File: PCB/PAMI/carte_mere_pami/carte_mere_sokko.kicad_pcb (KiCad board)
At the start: 2 copper layers, 78.5 x 66.5 mm, 34 parts, among them IC1 ESP32-S3-WROOM-1-N16R8, IC2 LDO_3.3V_bis, J1 Conn_01x08_Socket, J10 Conn_01x07_Socket, J11 Conn_01x07_Socket, J12 Conn_Servos, J14 LiDAR Connector, J2 Connector 5V, J3 Connector 3.3V, J4 Micro_USB_pads_USB3075-30-A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

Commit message: Routing nearly done
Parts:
- removed J6, J7: Conn_01x04_Socket, Connector_PinHeader_2.54mm:PinHeader_1x04_P2.54mm_Vertical
- moved TP_3.3V1 54.5 mm to (131.0, 82.5)
- moved D1 50.9 mm to (135.0, 89.5), turned to 90 degrees
- moved C9 49.6 mm to (135.0, 93.0), turned to -90 degrees
- moved TP_5V_USB1 48.5 mm to (138.0, 91.0)
- moved J3 43.5 mm to (135.0, 72.5), turned to -90 degrees
- moved C10 41.7 mm to (134.0, 85.0), turned to 180 degrees
- moved J1 38.0 mm to (181.5, 113.0), turned to 90 degrees
- moved J12 37.9 mm to (198.5, 80.0)
- moved J10 37.6 mm to (139.5, 101.3)
- moved C11 36.3 mm to (202.5, 87.5), turned to -90 degrees
- moved C7 34.9 mm to (205.0, 87.5), turned to -90 degrees
- moved J2 33.2 mm to (144.0, 72.5), turned to -90 degrees
- moved J5 32.5 mm to (181.5, 102.0), turned to 90 degrees
- moved C5 31.9 mm to (198.4, 109.5)
- moved J11 31.3 mm to (154.0, 101.4)
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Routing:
- net GND: track 0.00 -> 129.4 mm
- net MISO_LoRa: track 0.00 -> 67.0 mm
- net +3.3V: track 0.00 -> 63.0 mm
- net SS_LoRa: track 0.00 -> 57.1 mm
- net RS-SW_LoRa: track 0.00 -> 37.4 mm
- net EN_Right: track 0.00 -> 36.5 mm
- net RST_LoRa: track 0.00 -> 33.5 mm
- net Busy_LoRa: track 0.00 -> 32.3 mm
- net MOSI_LoRa: track 0.00 -> 31.7 mm
- net Boot_Button: track 0.00 -> 31.3 mm
- net DIO1_LoRa: track 0.00 -> 31.0 mm
- net CLK_LoRa: track 0.00 -> 30.7 mm
- net Data_servo: track 0.00 -> 30.4 mm
- net RX_LiDAR: track 0.00 -> 30.0 mm
- net EN_Left: track 0.00 -> 29.9 mm, vias 0 -> 2
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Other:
- outline, holes or cut-outs redrawn

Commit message: Smaller
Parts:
- added J6: Conn_01x04_Socket, Connector_PinHeader_2.54mm:PinHeader_1x04_P2.54mm_Vertical, F.Cu at (181.2, 114.0)
- added J7: Conn_01x04_Socket, Connector_PinHeader_2.54mm:PinHeader_1x04_P2.54mm_Vertical, F.Cu at (157.7, 114.0)
- moved TP_3.3V1 19.5 mm to (150.0, 78.0)
- moved J4 16.7 mm to (131.4, 83.4)
- moved C9 16.3 mm to (145.5, 80.5), turned to 0 degrees
- moved TP_5V_USB1 14.5 mm to (148.5, 81.0)
- moved IC2 12.3 mm to (142.5, 83.5), turned to 0 degrees
- moved D1 11.4 mm to (142.0, 80.5), turned to 180 degrees
- moved J10 10.6 mm to (133.0, 93.0)
- moved J11 10.6 mm to (147.5, 93.0)
- moved J1 7.11 mm to (176.0, 108.5)
- moved J5 7.11 mm to (176.0, 97.5)
- moved J8 7.11 mm to (153.0, 108.5)
- moved J9 7.11 mm to (153.0, 97.5)
- moved C10 4.95 mm to (137.5, 81.5), turned to -90 degrees
- moved C5 4.53 mm to (195.0, 112.5)
- moved C6 4.19 mm to (171.5, 112.0)
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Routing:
- net SS_LoRa: track 57.1 -> 4.55 mm
- net MISO_LoRa: track 67.0 -> 27.0 mm
- net EN_Left: track 29.9 -> 20.7 mm
- net MOSI_LoRa: track 31.7 -> 23.0 mm
- net STEP_Right: track 22.7 -> 15.3 mm
- net EN_Right: track 36.5 -> 29.7 mm
- net GND: track 129.4 -> 122.8 mm
- net DIR_Right: track 21.6 -> 15.4 mm
- net Net-(J7-Pin_2): track 0.00 -> 6.19 mm
- net USB_D+: track 28.6 -> 22.7 mm
- net USB_D-: track 28.6 -> 22.8 mm
- net Net-(J1-Pin_6): track 0.00 -> 5.75 mm
- net Net-(J7-Pin_4): track 0.00 -> 5.69 mm
- net Net-(J7-Pin_3): track 0.00 -> 5.69 mm
- net Net-(J7-Pin_1): track 0.00 -> 5.69 mm
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
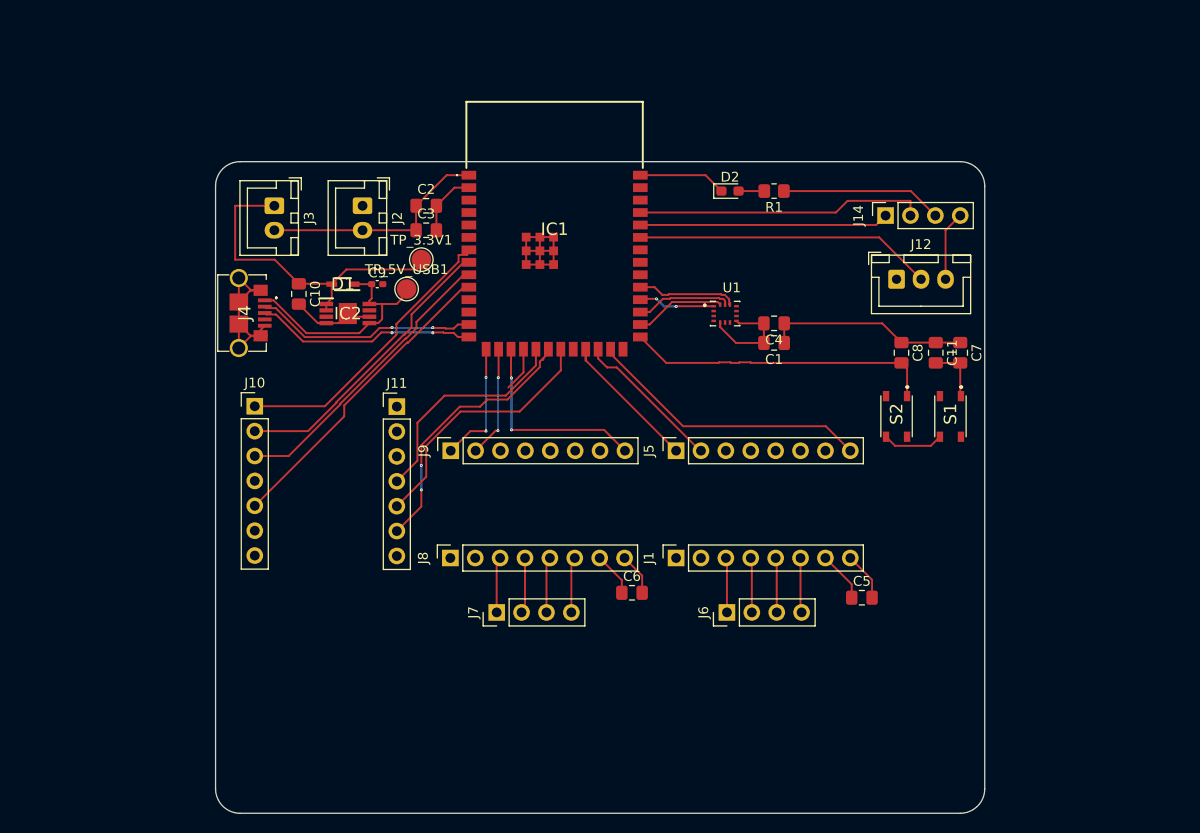
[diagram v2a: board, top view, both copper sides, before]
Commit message: PCB PAMI Nearly done, lack ground plane
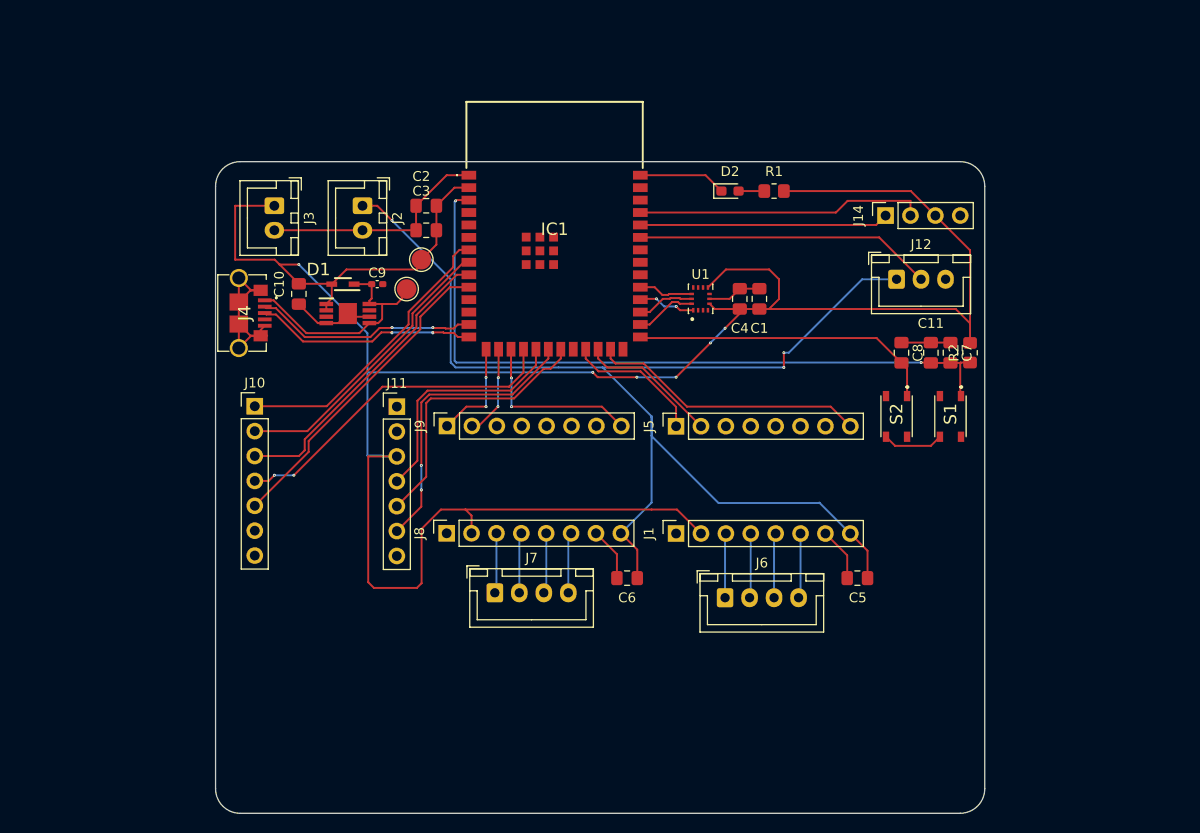
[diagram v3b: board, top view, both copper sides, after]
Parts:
- added R2: 10k, Resistor_SMD:R_0805_2012Metric_Pad1.20x1.40mm_HandSolder, F.Cu at (206.0, 87.5)
- J6, J7: value Conn_01x04_Socket -> Conn_01x04_Pin; footprint Connector_PinHeader_2.54mm:PinHeader_1x04_P2.54mm_Vertical -> Connector_JST:JST_XH_B4B-XH-A_1x04_P2.50mm_Vertical
- moved C1 4.74 mm to (184.5, 82.0), turned to -90 degrees
- moved C4 4.30 mm to (182.5, 82.0), turned to -90 degrees
- moved U1 2.92 mm to (178.5, 82.0), turned to 90 degrees
- moved J8 2.55 mm to (152.6, 105.9)
- moved J9 2.55 mm to (152.6, 95.0)
- moved J1 2.50 mm to (176.0, 106.0)
- moved J5 2.50 mm to (176.0, 95.0)
- moved C5 2.05 mm to (194.5, 110.5)
- moved J7 2.01 mm to (157.5, 112.0), turned to 0 degrees
- moved C6 1.58 mm to (171.0, 110.5)
- moved J6 1.51 mm to (181.0, 112.5), turned to 0 degrees
- moved C7 1.00 mm to (204.0, 87.5)
- moved C11 0.50 mm to (202.0, 87.5)
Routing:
- net +3.3V: track 67.4 -> 243.3 mm, vias 0 -> 6
- net +5V: track 9.23 -> 128.2 mm, vias 0 -> 3
- net Enable_BTN: track 5.92 -> 74.0 mm, vias 0 -> 2
- net GND: track 122.8 -> 89.9 mm
- net SS_LoRa: track 4.55 -> 34.4 mm, vias 0 -> 2
- net SS_IMU: track 10.3 -> 5.61 mm
- net CLK_IMU: track 9.75 -> 5.86 mm
- net MOSI_IMU: track 9.21 -> 6.26 mm
- net EN_Left: track 20.7 -> 17.9 mm
- net CLK_LoRa: track 27.5 -> 29.9 mm
- net STEP_Left: track 11.5 -> 9.36 mm
- net DIR_Left: track 12.8 -> 10.7 mm
- net MISO_IMU: track 7.85 -> 5.95 mm
- net EN_Right: track 29.7 -> 28.3 mm
- net MOSI_LoRa: track 23.0 -> 24.3 mm
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
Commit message: V2 PAMI Motherboard
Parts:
- J12: footprint Connector_JST:JST_XH_B3B-XH-A_1x03_P2.50mm_Vertical -> Connector_PinHeader_2.00mm:PinHeader_1x03_P2.00mm_Vertical
- moved S2 16.8 mm to (197.2, 77.2), turned to 90 degrees
- moved S1 16.8 mm to (203.2, 77.2), turned to 90 degrees
- moved J14 13.9 mm to (183.4, 73.7)
- moved J12 11.7 mm to (187.0, 78.0), turned to 90 degrees
- moved R2 6.05 mm to (201.2, 83.8), turned to -90 degrees
- moved R1 5.06 mm to (181.0, 70.2)
- moved C11 4.96 mm to (205.2, 83.8), turned to 90 degrees
- moved D2 4.81 mm to (176.8, 70.2)
- moved C8 4.37 mm to (196.8, 83.8), turned to 90 degrees
- moved C7 3.82 mm to (203.2, 83.8), turned to 90 degrees
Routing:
- net +3.3V: track 243.3 -> 61.1 mm, vias 6 -> 0
- net GND: track 89.9 -> 111.8 mm, vias 0 -> 9
- net RX_LiDAR: track 30.0 -> 14.4 mm
- net TX_LiDAR: track 25.4 -> 11.4 mm
- net Data_servo: track 30.4 -> 17.6 mm
- net +5V: track 128.2 -> 123.1 mm
- net Boot_Button: track 31.4 -> 28.7 mm
- net Enable_BTN: track 74.0 -> 75.5 mm
- added copper zone on F.Cu, net +3.3V
- added copper zone on B.Cu, net GND
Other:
- board size 78.5 x 66.5 mm -> 78.5 x 54 mm
- board text added: "BOOT"
- board text added: "Motherboard PAMI v2 2024/25"
- board text added: "RESET"

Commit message: Fix PCB
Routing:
- net MOSI_LoRa: track 24.3 -> 27.0 mm
- net GND: track 111.8 -> 114.0 mm, vias 9 -> 11
- net MISO_LoRa: track 28.3 -> 27.1 mm
- net +3.3V: track 61.1 -> 61.8 mm
- net +5V: track 123.1 -> 123.8 mm
- net USB_D+: track 22.7 -> 23.2 mm

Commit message: Improve PAMI motherboard
Change footprint for the servo header
link the 3.3 plane to improve reliability
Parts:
- J12: footprint Connector_PinHeader_2.00mm:PinHeader_1x03_P2.00mm_Vertical -> Connector_PinHeader_2.54mm:PinHeader_1x03_P2.54mm_Vertical
- moved J12 1.07 mm to (186.0, 77.8)
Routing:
- net +3.3V: track 61.8 -> 37.7 mm, vias 0 -> 2
- net GND: track 114.0 -> 92.7 mm, vias 11 -> 19
- net +5V: track 123.8 -> 124.4 mm
- net Data_servo: track 17.6 -> 17.0 mm
- added copper zone on F.Cu, net GND

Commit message: Update hole position
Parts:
- moved J14 1.76 mm to (184.9, 72.7)
- moved J1 0.25 mm to (176.0, 106.2)
- moved J8 0.25 mm to (152.6, 106.2)
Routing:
- net TX_LiDAR: track 11.4 -> 13.3 mm
- net RX_LiDAR: track 14.4 -> 16.2 mm
- net GND: track 92.7 -> 91.2 mm
- net +3.3V: track 37.7 -> 38.7 mm
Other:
- board text added: "M1A"
- board text added: "M1B"
- board text added: "M2A"
- board text added: "M2B"
